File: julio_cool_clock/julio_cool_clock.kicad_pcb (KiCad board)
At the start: 2 copper layers, 140 x 90 mm, 4 parts

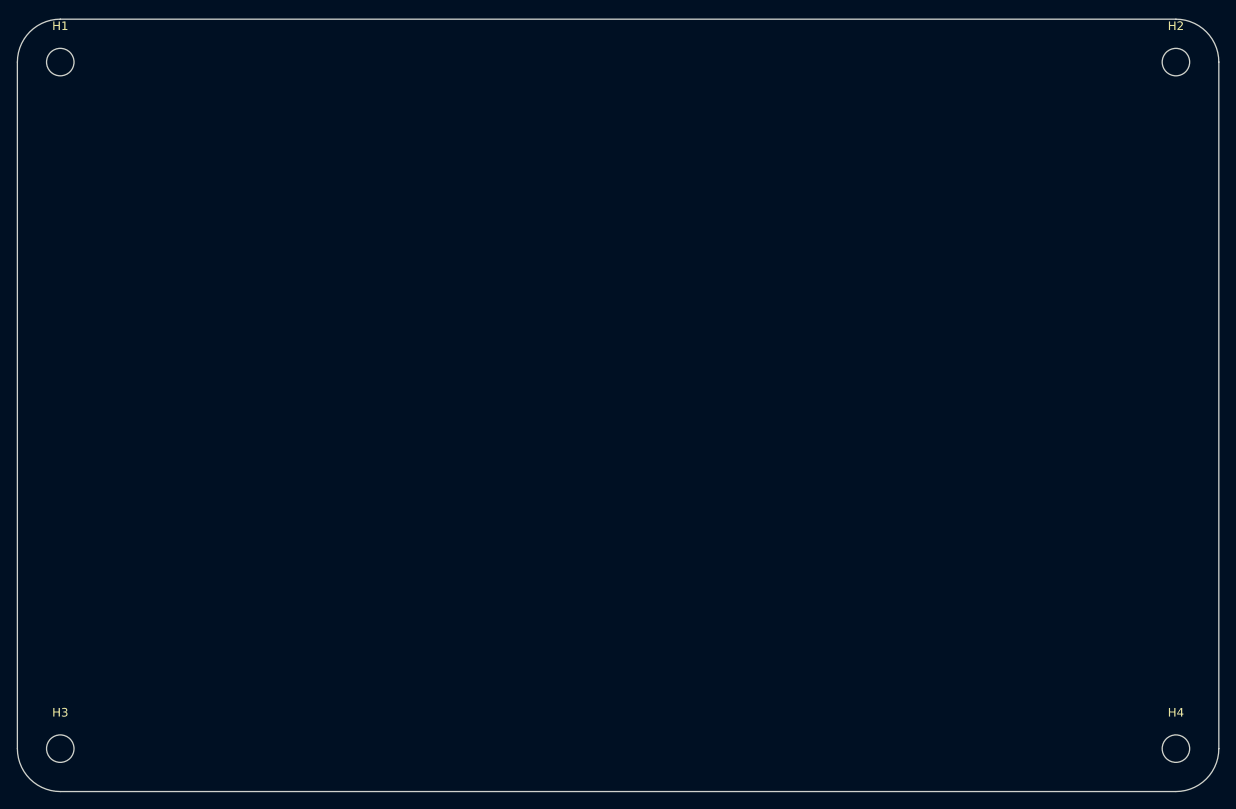
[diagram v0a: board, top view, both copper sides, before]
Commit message: Design Commit 4.2
Arranged components from schematic onto PCB.
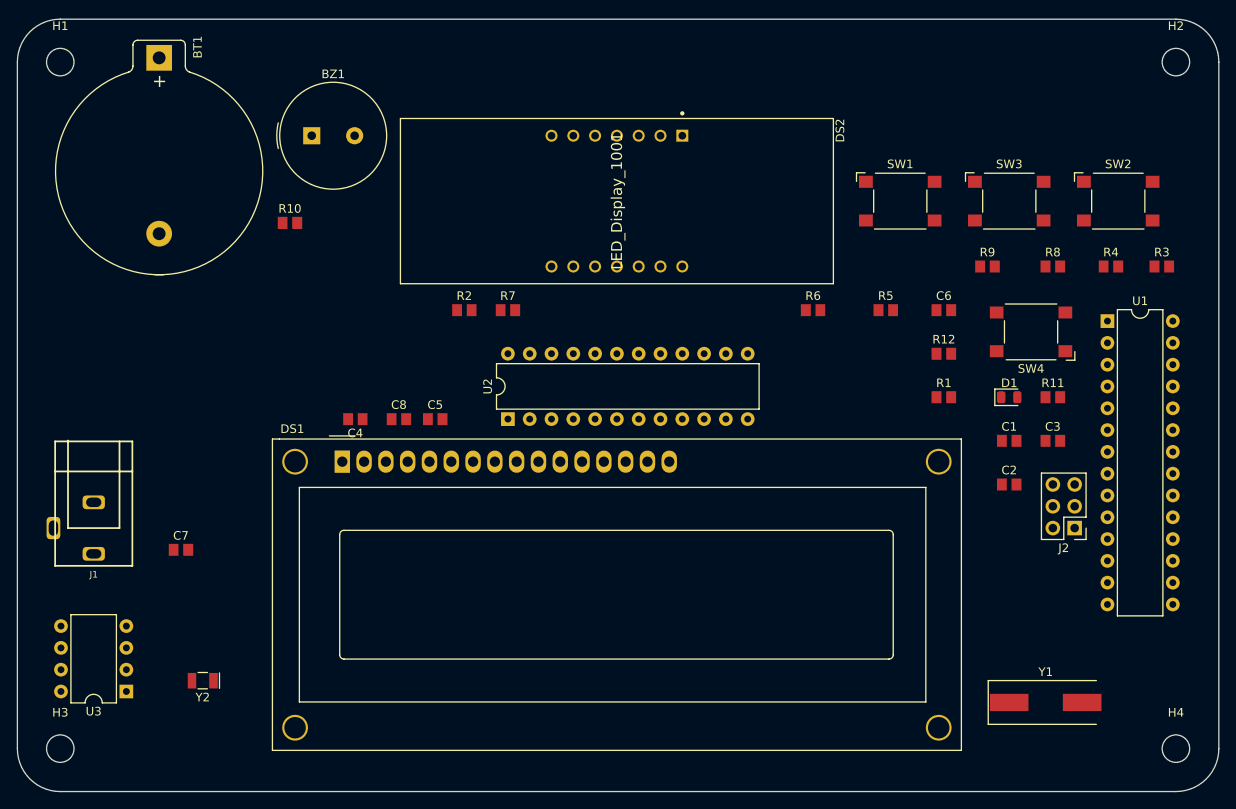
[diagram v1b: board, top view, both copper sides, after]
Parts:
- added BT1: Battery_Cell, footprints:BatteryHolder_Keystone_106_1x20mm, F.Cu at (96.5, 59.5)
- added BZ1: Buzzer, footprints:Buzzer_TDK_PS1240P02BT_D12.2mm_H6.5mm, F.Cu at (114.3, 68.6)
- added C1: C_10uf, footprints:C_0805_2012Metric, F.Cu at (195.6, 104.1)
- added C2: C_22pf, footprints:C_0805_2012Metric, F.Cu at (195.6, 109.2)
- added C3: C_22pf, footprints:C_0805_2012Metric, F.Cu at (200.7, 104.1)
- added C4: C_0805_0.1uf, footprints:C_0805_2012Metric, F.Cu at (119.4, 101.6)
- added C5: C_0805_10uf, footprints:C_0805_2012Metric, F.Cu at (128.7, 101.6)
- added C6: C_0.1uf, footprints:C_0805_2012Metric, F.Cu at (188.0, 88.9)
- added C7: C_0805_1uf, footprints:C_0805_2012Metric, F.Cu at (99.1, 116.8)
- added C8: C_0805_0.1uf, footprints:C_0805_2012Metric, F.Cu at (124.5, 101.6)
- added D1: LED_0805, footprints:LED_0805_2012Metric, F.Cu at (195.6, 99.1)
- added DS1: TC1602A-01T, footprints:TC1602A-01T, F.Cu at (117.9, 106.6)
- added DS2: LED_Display_1001, footprints:Adafruit-1001-0-0-MFG, F.Cu at (149.9, 76.2)
- added J1: PJ-102AH, footprints:PJ-102AH, F.Cu at (88.9, 114.3)
- added J2: Conn_02x03_Odd_Even, footprints:PinHeader_2x03_P2.54mm_Vertical, F.Cu at (203.2, 114.3)
- added R1: R_2.2K, footprints:R_0805_2012Metric, F.Cu at (188.0, 99.1)
- added R10: R_0805_47, footprints:R_0805_2012Metric, F.Cu at (111.8, 78.7)
- added R11: R_0805_4.7K, footprints:R_0805_2012Metric, F.Cu at (200.7, 99.1)
- added R12: R_0805_4.7K, footprints:R_0805_2012Metric, F.Cu at (188.0, 94.0)
- added R2: R_0805_22K, footprints:R_0805_2012Metric, F.Cu at (132.1, 88.9)
- added R3: R_0805_4.7K, footprints:R_0805_2012Metric, F.Cu at (213.4, 83.8)
- added R4: R_0805_4.7K, footprints:R_0805_2012Metric, F.Cu at (207.4, 83.8)
- added R5: R_10K, footprints:R_0805_2012Metric, F.Cu at (181.2, 88.9)
- added R6: R_0805_10K, footprints:R_0805_2012Metric, F.Cu at (172.7, 88.9)
- added R7: R_0805_47, footprints:R_0805_2012Metric, F.Cu at (137.2, 88.9)
- added R8: R_0805_10K, footprints:R_0805_2012Metric, F.Cu at (200.7, 83.8)
- added R9: R_0805_10K, footprints:R_0805_2012Metric, F.Cu at (193.0, 83.8)
- added SW1: Omron_B3F_SPST, footprints:SW_SPST_Omron_B3FS-100xP, F.Cu at (182.9, 76.2)
- added SW2: Omron_B3F_SPST, footprints:SW_SPST_Omron_B3FS-100xP, F.Cu at (208.3, 76.2)
- added SW3: Omron_B3F_SPST, footprints:SW_SPST_Omron_B3FS-100xP, F.Cu at (195.6, 76.2)
- added SW4: Omron_B3F_SPST, footprints:SW_SPST_Omron_B3FS-100xP, F.Cu at (198.1, 91.4)
- added U1: ATmega328-PU, footprints:DIP-28_W7.62mm, F.Cu at (207.0, 90.2)
- added U2: MAX7219, footprints:DIP-24_W7.62mm, F.Cu at (137.2, 101.6)
- added U3: DS1307_DIP-8, footprints:DIP-8_W7.62mm, F.Cu at (92.7, 133.3)
- added Y1: Crystal_16MHz, footprints:Crystal_SMD_HC49-SD, F.Cu at (199.8, 134.6)
- added Y2: Crystal_32768Hz, footprints:Crystal_SMD_2Pin_3.2x1.5mm, F.Cu at (101.6, 132.1)
